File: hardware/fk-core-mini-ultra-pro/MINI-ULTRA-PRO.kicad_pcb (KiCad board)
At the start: 2 copper layers, 26.2 x 105.4 mm, 69 parts, among them J1 S2B-PH-SM4-TB, J2 MICRO-USB, J3 RF-SMA-EDGE, J4 CONN-HDR-1x19, J5 CONN-HDR-1x19, J6 CONN-HDR-2x5, M1 MOUNT_HOLE, M2 MOUNT_HOLE, M3 MOUNT_HOLE, M4 MOUNT_HOLE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

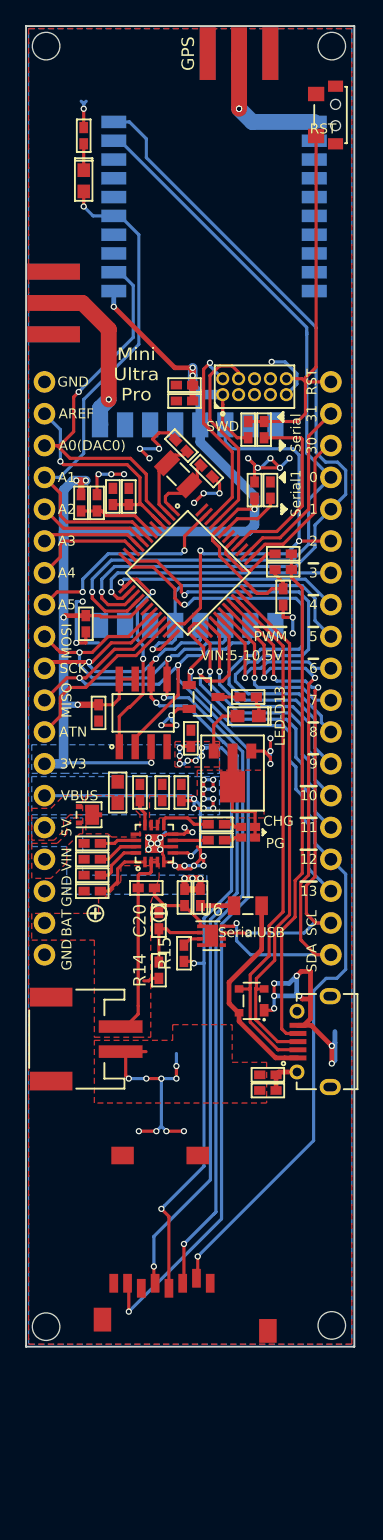
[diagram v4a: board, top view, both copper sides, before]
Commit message: Some layout tweaks, also adding a module header.
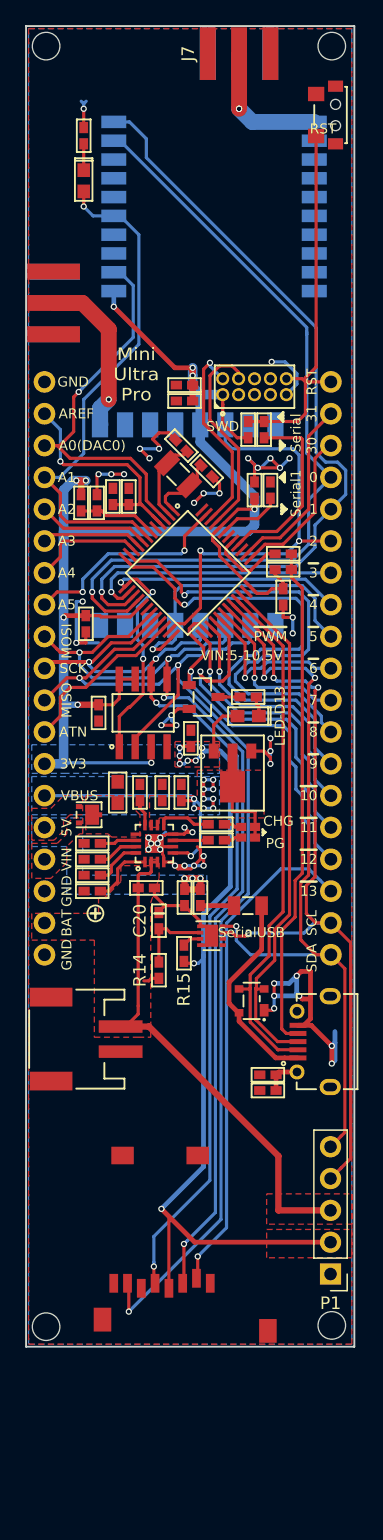
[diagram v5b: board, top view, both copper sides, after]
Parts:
- removed GPS: RF-SMA-EDGE, RocketScreamKicadLibrary:RF-SMA-EDGE
- added J7: RF-SMA-EDGE, RocketScreamKicadLibrary:RF-SMA-EDGE, F.Cu at (143.8, 50.0)
- added P1: CONN-HDR-MODULE, fk-core-mini-ultra-pro:Socket_Strip_Straight_1x05_Pitch2.54mm, F.Cu at (151.1, 147.4)
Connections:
- M7 pad 2: /D12 -> /D13
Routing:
- net /D12: track 69.4 -> 30.0 mm, vias 2 -> 1
- net /D13: track 31.8 -> 69.4 mm, vias 1 -> 2
- net VBAT: track 16.2 -> 41.6 mm
- net /SCL: track 40.8 -> 62.7 mm
- net GND: track 112.1 -> 94.6 mm, vias 55 -> 46
- net /SDA: track 46.4 -> 62.3 mm
- net 3V3: track 190.9 -> 205.5 mm

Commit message: Adding header for modules to PCB.
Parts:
- removed LOGO1: LOGO-ROCKET-SCREAM, RocketScreamKicadLibrary:LOGO-ROCKET-SCREAM_Vertical_Small
- removed LOGO2: LOGO-OSHW, RocketScreamKicadLibrary:LOGO-OSHW_Small
- removed LOGO3: LOGO-KICAD, RocketScreamKicadLibrary:LOGO-KICAD_XSmall
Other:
- board text removed: "868MHZ"
- board text removed: "915MHZ"
- board text removed: "Made With"
- board text removed: "Mini Ultra Pro"
- board text removed: "Mini Ultra Pro 11-2015 0v20"
- board text removed: "RFM69"
- board text removed: "RFM95"
- board text removed: "SerialUSB"

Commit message: Pull ups on SDA/SCL and some tweaks.
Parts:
- added R17: 4.7K, RocketScreamKicadLibrary:RES-0603, F.Cu at (145.8, 114.8)
- added R18: 4.7K, RocketScreamKicadLibrary:RES-0603, F.Cu at (145.8, 116.5)
- moved F1 7.20 mm to (138.2, 121.4), turned to 270 degrees
- moved C20 5.80 mm to (143.2, 119.3)
- moved R14 5.17 mm to (141.8, 120.3)
- moved U6 3.93 mm to (145.5, 120.9)
- moved R15 3.86 mm to (143.2, 122.5)
- moved R5 3.76 mm to (145.8, 136.5)
- moved J2 3.53 mm to (149.9, 132.4)
- moved C18 3.51 mm to (145.8, 135.0)
- moved D3 3.20 mm to (148.0, 125.8)
- moved P1 1.20 mm to (151.1, 148.6)
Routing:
- net GND: track 94.6 -> 69.4 mm, vias 46 -> 43
- net VBAT: track 41.6 -> 56.1 mm
- net Net-(J2-Pad4): track 40.4 -> 45.5 mm
- net /SDA: track 62.3 -> 57.5 mm, vias 3 -> 1
- net 3V3: track 205.5 -> 210.1 mm, vias 18 -> 19
- net VUSB: track 16.6 -> 20.2 mm
- net /USB+: track 41.3 -> 44.8 mm
- net /USB-: track 41.9 -> 45.4 mm
- net Net-(C20-Pad1): track 6.07 -> 3.24 mm
- net /SCL: track 62.7 -> 60.2 mm, vias 3 -> 1
- net Net-(F1-Pad1): track 2.69 -> 4.03 mm
- net /D13: track 69.4 -> 68.8 mm
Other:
- net class Default: clearance 0.19 -> 0.1524
- rule trace_clearance: 0.19 -> 0.1524
- board text added: "A0"
- board text removed: "A0(DAC0)"

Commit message: Changing some footprints.
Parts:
- added M5, M6: FIDUCIAL, RocketScreamKicadLibrary:FIDUCIAL-1MM, F.Cu at (139.9, 163.3)
- C20: footprint RocketScreamKicadLibrary:CAP-0402 -> RocketScreamKicadLibrary:CAP-0603
- R14, R15, R16: footprint RocketScreamKicadLibrary:RES-0402 -> RocketScreamKicadLibrary:RES-0603
- moved R14 0.76 mm to (141.3, 121.0)
- moved R15 0.32 mm to (143.1, 122.8)
- moved C20 0.14 mm to (143.1, 119.2)
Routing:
- net 3V3: track 210.1 -> 210.9 mm
- net Net-(C20-Pad1): track 3.24 -> 3.89 mm
